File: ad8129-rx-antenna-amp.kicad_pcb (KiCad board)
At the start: 2 copper layers, 50 x 42 mm, 43 parts, among them J1 ANT, J2 TUNE, J3 TRX, T1 Transformer_1P_1S, U1 AD8129, U2 L78L06_SO8

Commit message: FIX: change project file names to match GitHub project name
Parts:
- C1, C10, C11, C12, C13, C2, C3, C4, C5, C6, C7, C8, C9: footprint AD8129 Preamp Board:C_0805_2012Metric -> ad8129-rx-antenna-amp:C_0805_2012Metric
- D1, D2, D3, D4: footprint AD8129 Preamp Board:D_SOD-323 -> ad8129-rx-antenna-amp:D_SOD-323
- D5, D6, D7, D8: footprint AD8129 Preamp Board:D_SOD-123 -> ad8129-rx-antenna-amp:D_SOD-123
- H1, H2, H3, H4: footprint AD8129 Preamp Board:MountingHole_3.2mm_M3 -> ad8129-rx-antenna-amp:MountingHole_3.2mm_M3
- J1: footprint AD8129 Preamp Board:WirePad_3_0.8_1.5 -> ad8129-rx-antenna-amp:WirePad_3_0.8_1.5
- J2: footprint AD8129 Preamp Board:WirePad_1_0.8_1.5 -> ad8129-rx-antenna-amp:WirePad_1_0.8_1.5
- J3: footprint AD8129 Preamp Board:SMA_Samtec_SMA-J-P-X-ST-EM1_EdgeMount -> ad8129-rx-antenna-amp:SMA_Samtec_SMA-J-P-X-ST-EM1_EdgeMount
- L1, L2, L3, L4: footprint AD8129 Preamp Board:L_1812_4532Metric_Pad1.30x3.40mm_HandSolder -> ad8129-rx-antenna-amp:L_1812_4532Metric_Pad1.30x3.40mm_HandSolder
- R1, R2, R3, R4, R5, R6, R7, R8: footprint AD8129 Preamp Board:R_0805_2012Metric -> ad8129-rx-antenna-amp:R_0805_2012Metric
- T1: footprint AD8129 Preamp Board:TR-FT-50-43-1P-1S-Isolated -> ad8129-rx-antenna-amp:TR-FT-50-43-1P-1S-Isolated
- U1: footprint AD8129 Preamp Board:SOIC-8_3.9x4.9mm_P1.27mm -> ad8129-rx-antenna-amp:SOIC-8_3.9x4.9mm_P1.27mm

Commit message: ADD: version and date variables
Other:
- board text added: "AD8129 RX ANTENNA AMP Design: DL2KQ Routing: R2AXZ Version ${VERSION} ${DATE}"
- board text removed: "AD8129 RX ANTENNA AMP Design: DL2KQ Routing: R2AXZ Version 1.0 7 Jul 2022"
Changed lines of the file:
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@@
     )
   )
+  (property "DATE" "07 Jul 2022")
+  (property "VERSION" "1.0")
   (net 0 "")
   (net 1 "Net-(C1-Pad1)")
@@
     (effects (font (size 1 1) (thickness 0.2)))
   )
-  (gr_text "AD8129 RX ANTENNA AMP\nDesign: DL2KQ\nRouting: R2AXZ\nVersion 1.0\n7 Jul 2022" (at 129 117.75) (layer "F.SilkS")
+  (gr_text "AD8129 RX ANTENNA AMP\nDesign: DL2KQ\nRouting: R2AXZ\nVersion ${VERSION}\n${DATE}" (at 129 117.75) (layer "F.SilkS")
     (effects (font (size 1 1) (thickness 0.2)) (justify left))
   )

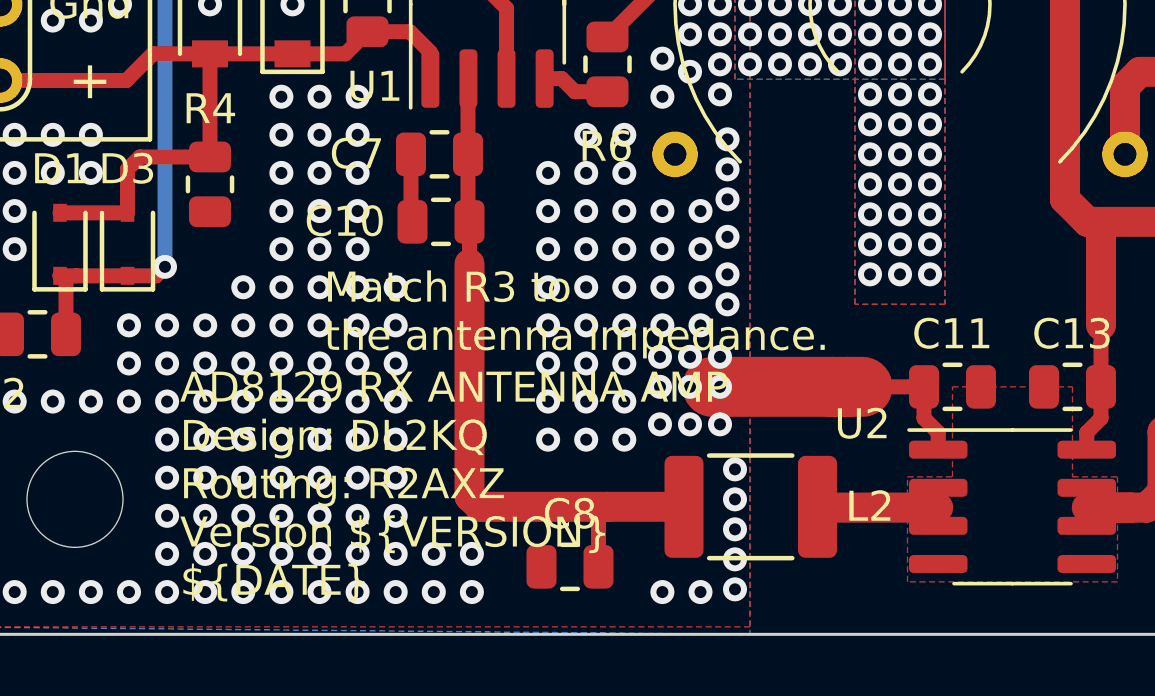
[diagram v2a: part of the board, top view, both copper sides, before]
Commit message: FIX: variables case, board labels location
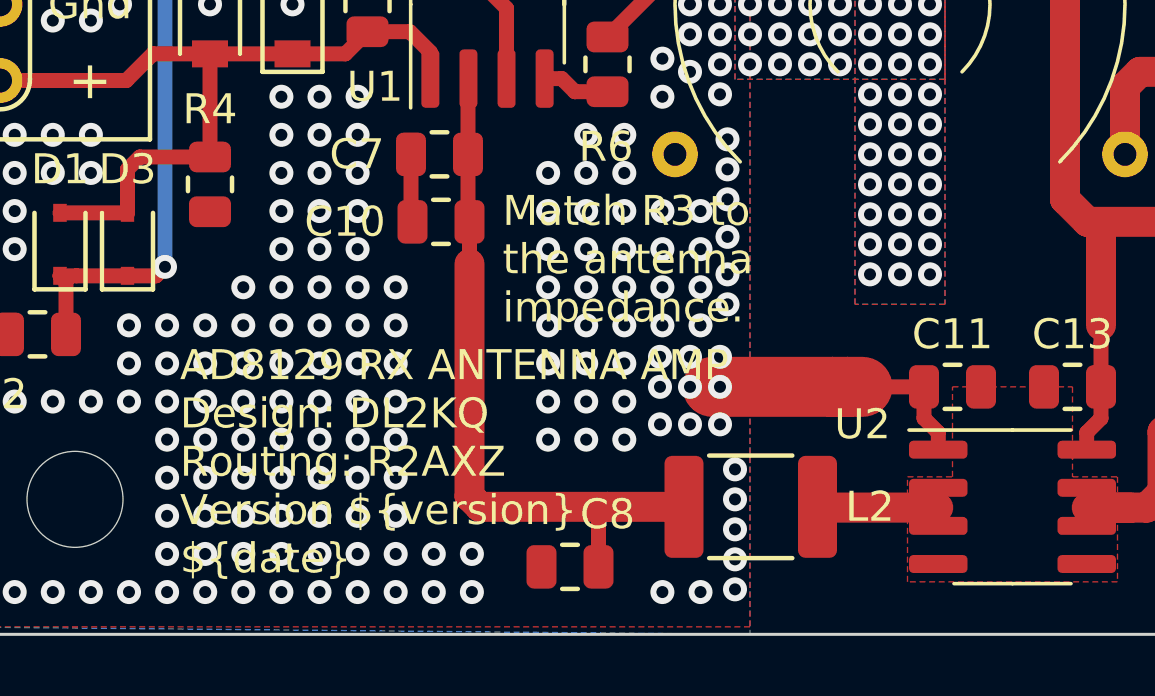
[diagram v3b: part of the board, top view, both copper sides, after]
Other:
- board text added: "AD8129 RX ANTENNA AMP Design: DL2KQ Routing: R2AXZ Version ${version} ${date}"
- board text removed: "AD8129 RX ANTENNA AMP Design: DL2KQ Routing: R2AXZ Version ${VERSION} ${DATE}"
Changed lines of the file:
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@@
     )
   )
-  (property "DATE" "07 Jul 2022")
-  (property "VERSION" "1.0")
+  (property "date" "07 Jul 2022")
+  (property "version" "cda1a58")
   (net 0 "")
   (net 1 "Net-(C1-Pad1)")
@@
     (property "Sheetname" "")
     (attr smd)
-    (fp_text reference "C8" (at 0 1.75) (layer "F.SilkS")
-      (effects (font (size 1 1) (thickness 0.15)))
-    )
-    (fp_text value "100n" (at 0 1.68) (layer "F.Fab")
+    (fp_text reference "C8" (at -1.25 1.75) (layer "F.SilkS")
+      (effects (font (size 1 1) (thickness 0.15)))
+    )
+    (fp_text value "100n" (at 0 1.68) (layer "F.Fab") hide
       (effects (font (size 1 1) (thickness 0.15)))
     )
@@
     (effects (font (size 1 1) (thickness 0.2)) (justify left))
   )
-  (gr_text "Match R3 to \nthe antenna impedance." (at 133.8 112) (layer "F.SilkS")
+  (gr_text "Match R3 to \nthe antenna\nimpedance." (at 139.75 110.25) (layer "F.SilkS")
     (effects (font (size 1 1) (thickness 0.2)) (justify left))
   )
@@
     (effects (font (size 1 1) (thickness 0.2)))
   )
-  (gr_text "AD8129 RX ANTENNA AMP\nDesign: DL2KQ\nRouting: R2AXZ\nVersion ${VERSION}\n${DATE}" (at 129 117.75) (layer "F.SilkS")
+  (gr_text "AD8129 RX ANTENNA AMP\nDesign: DL2KQ\nRouting: R2AXZ\nVersion ${version}\n${date}" (at 129 117) (layer "F.SilkS")
     (effects (font (size 1 1) (thickness 0.2)) (justify left))
   )
